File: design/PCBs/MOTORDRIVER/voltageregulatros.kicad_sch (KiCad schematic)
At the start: 0 parts

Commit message: worked on motor pcb
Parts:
- added U2: ADP1108AN-3.3, Package_DIP:DIP-8_W7.62mm, symbol Regulator_Switching:ADP1108AN-3.3
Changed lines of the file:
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@@
 	(generator_version "8.0")
 	(paper "A4")
+	(global_label "3.3V"
+		(shape input)
+		(at 143.51 77.47 0)
+		(fields_autoplaced yes)
+		(effects
+			(font
+				(size 1.27 1.27)
+			)
+			(justify left)
+		)
+		(property "Intersheetrefs" "${INTERSHEET_REFS}"
+			(at 150.5409 77.47 0)
+			(effects
+				(font
+					(size 1.27 1.27)
+				)
+				(justify left)
+				(hide yes)
+			)
+		)
+	)
+	(global_label "12V"
+		(shape input)
+		(at 125.73 81.28 180)
+		(fields_autoplaced yes)
+		(effects
+			(font
+				(size 1.27 1.27)
+			)
+			(justify right)
+		)
+		(property "Intersheetrefs" "${INTERSHEET_REFS}"
+			(at 119.7661 81.28 0)
+			(effects
+				(font
+					(size 1.27 1.27)
+				)
+				(justify right)
+				(hide yes)
+			)
+		)
+	)
+	(symbol
+		(lib_id "Regulator_Switching:ADP1108AN-3.3")
+		(at 142.24 96.52 0)
+		(unit 1)
+		(exclude_from_sim no)
+		(in_bom yes)
+		(on_board yes)
+		(dnp no)
+		(fields_autoplaced yes)
+		(property "Reference" "U2"
+			(at 125.73 89.5855 0)
+			(effects
+				(font
+					(size 1.27 1.27)
+				)
+			)
+		)
+		(property "Value" "ADP1108AN-3.3"
+			(at 125.73 92.1255 0)
+			(effects
+				(font
+					(size 1.27 1.27)
+				)
+			)
+		)
+		(property "Footprint" "Package_DIP:DIP-8_W7.62mm"
+			(at 143.51 105.41 0)
+			(effects
+				(font
+					(size 1.27 1.27)
+				)
+				(justify left)
+				(hide yes)
+			)
+		)
+		(property "Datasheet" "https://www.analog.com/media/en/technical-documentation/data-sheets/ADP1108.pdf"
+			(at 137.16 81.28 0)
+			(effects
+				(font
+					(size 1.27 1.27)
+				)
+				(hide yes)
+			)
+		)
+		(property "Description" "Micropower DC-DC converter, step-up or step-down operation, 2V-30Vin, 3.3V fixed output voltage, DIP-8"
+			(at 142.24 96.52 0)
+			(effects
+				(font
+					(size 1.27 1.27)
+				)
+				(hide yes)
+			)
+		)
+		(pin "7"
+		)
+		(pin "1"
+		)
+		(pin "2"
+		)
+		(pin "5"
+		)
+		(pin "4"
+		)
+		(pin "3"
+		)
+		(pin "6"
+		)
+		(pin "8"
+		)
+		(instances
+			(project ""
+				(path "/c7634e88-16d1-45ec-9aac-9c841e03cf6d/40fe2217-7020-4fd5-b361-1423767f0697"
+					(reference "U2")
+					(unit 1)
+				)
+			)
+		)
+	)
 )

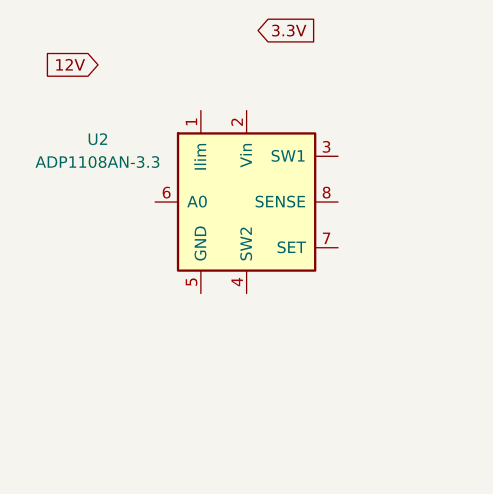
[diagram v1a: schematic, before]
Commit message: moved controller pcb to a single unified pcb, added more work on motordriver
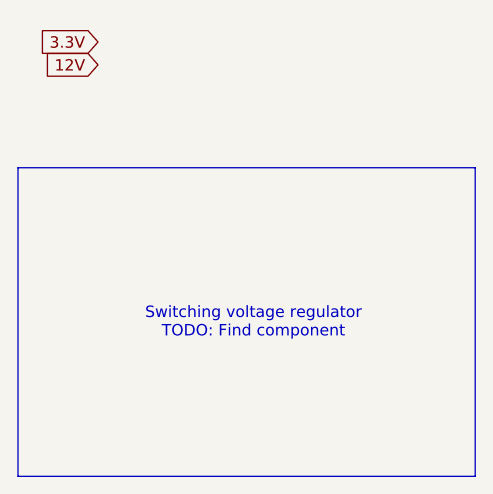
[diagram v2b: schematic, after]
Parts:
- removed U2: ADP1108AN-3.3, Package_DIP:DIP-8_W7.62mm, symbol Regulator_Switching:ADP1108AN-3.3
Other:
- note added: "Switching voltage regulator TODO: Find component"
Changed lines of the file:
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@@
 	(generator_version "8.0")
 	(paper "A4")
+	(rectangle
+		(start 116.84 92.71)
+		(end 167.64 127)
+		(stroke
+			(width 0)
+			(type default)
+		)
+		(fill
+			(type none)
+		)
+	)
+	(text "Switching voltage regulator\nTODO: Find component"
+		(exclude_from_sim no)
+		(at 143.002 109.982 0)
+		(effects
+			(font
+				(size 1.27 1.27)
+			)
+		)
+	)
 	(global_label "3.3V"
 		(shape input)
-		(at 143.51 77.47 0)
+		(at 125.73 78.74 180)
 		(fields_autoplaced yes)
 		(effects
@@
 				(size 1.27 1.27)
 			)
-			(justify left)
+			(justify right)
 		)
 		(property "Intersheetrefs" "${INTERSHEET_REFS}"
-			(at 150.5409 77.47 0)
+			(at 118.6991 78.74 0)
 			(effects
 				(font
 					(size 1.27 1.27)
 				)
-				(justify left)
+				(justify right)
 				(hide yes)
 			)
@@
 			)
 		)
-	)
-	(symbol
-		(lib_id "Regulator_Switching:ADP1108AN-3.3")
-		(at 142.24 96.52 0)
-		(unit 1)
-		(exclude_from_sim no)
-		(in_bom yes)
-		(on_board yes)
-		(dnp no)
-		(fields_autoplaced yes)
-		(property "Reference" "U2"
-			(at 125.73 89.5855 0)
-			(effects
-				(font
-					(size 1.27 1.27)
-				)
-			)
-		)
-		(property "Value" "ADP1108AN-3.3"
-			(at 125.73 92.1255 0)
-			(effects
-				(font
-					(size 1.27 1.27)
-				)
-			)
-		)
-		(property "Footprint" "Package_DIP:DIP-8_W7.62mm"
-			(at 143.51 105.41 0)
-			(effects
-				(font
-					(size 1.27 1.27)
-				)
-				(justify left)
-				(hide yes)
-			)
-		)
-		(property "Datasheet" "https://www.analog.com/media/en/technical-documentation/data-sheets/ADP1108.pdf"
-			(at 137.16 81.28 0)
-			(effects
-				(font
-					(size 1.27 1.27)
-				)
-				(hide yes)
-			)
-		)
-		(property "Description" "Micropower DC-DC converter, step-up or step-down operation, 2V-30Vin, 3.3V fixed output voltage, DIP-8"
-			(at 142.24 96.52 0)
-			(effects
-				(font
-					(size 1.27 1.27)
-				)
-				(hide yes)
-			)
-		)
-		(pin "7"
-		)
-		(pin "1"
-		)
-		(pin "2"
-		)
-		(pin "5"
-		)
-		(pin "4"
-		)
-		(pin "3"
-		)
-		(pin "6"
-		)
-		(pin "8"
-		)
-		(instances
-			(project ""
-				(path "/c7634e88-16d1-45ec-9aac-9c841e03cf6d/40fe2217-7020-4fd5-b361-1423767f0697"
-					(reference "U2")
-					(unit 1)
-				)
-			)
-		)

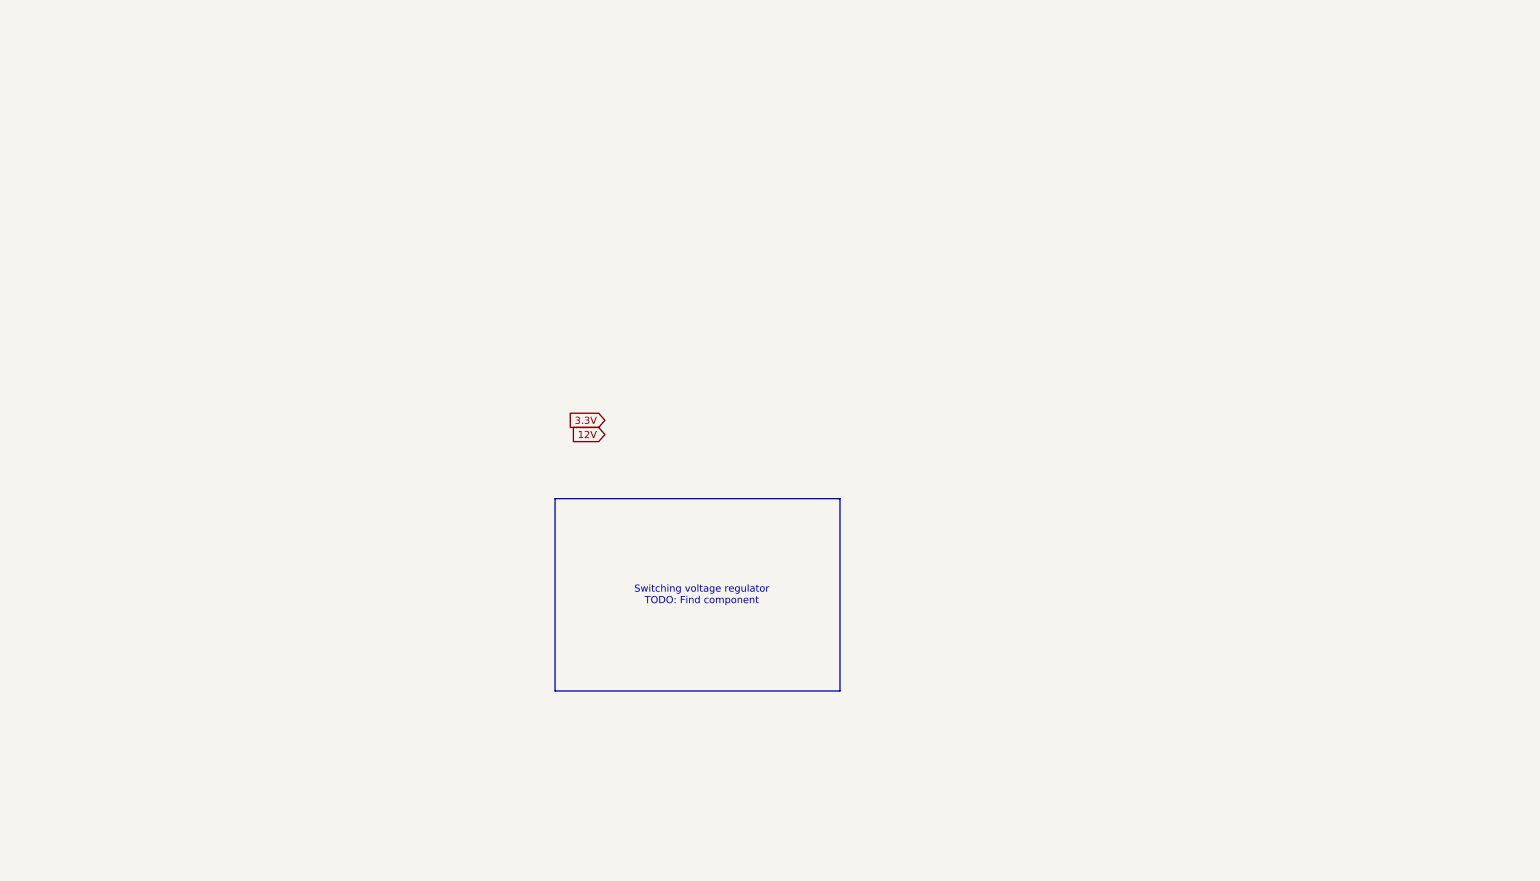
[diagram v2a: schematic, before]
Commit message: 12 to 3.3 LDO added, temporary 5 to 12 reg added
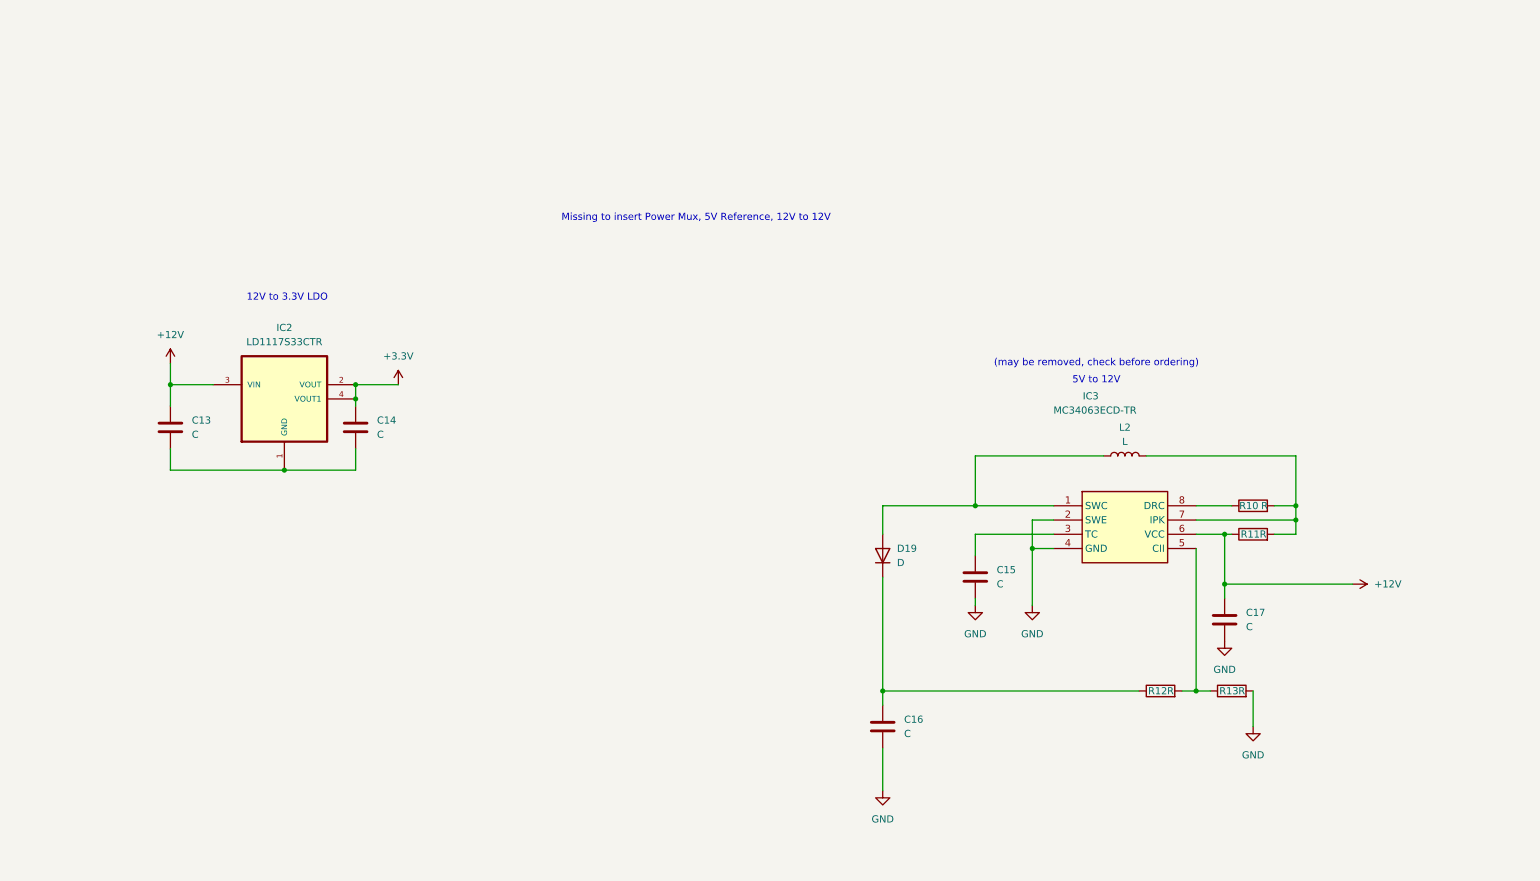
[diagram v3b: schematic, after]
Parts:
- added C13, C14, C15, C16, C17: C, symbol Device:C
- added D19: D, symbol Device:D
- added IC2: LD1117S33CTR, LD1117S33CTR:SOT223, symbol LD1117S33CTR:LD1117S33CTR
- added IC3: MC34063ECD-TR, SOIC127P600X175-8N, symbol MC34063ECD-TR:MC34063ECD-TR
- added L2: L, symbol Device:L
- added R10, R11, R12, R13: R, symbol Device:R
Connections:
- new net: C13.2, C14.2, IC2.1 (GND)
- new net: C16.1, D19.1 (K), R12.1
- new net: D19.2 (A), IC3.1 (SWC), L2.1
- new net: C15.1, IC3.3 (TC)
- new net: IC3.5 (CII), R12.2, R13.1
- new net: IC3.7 (IPK), L2.2, R10.2, R11.2
- new net: IC3.8 (DRC), R10.1
- new net +12V: C13.1, C17.1, IC2.3 (VIN), IC3.6 (VCC), R11.1
- new net +3.3V: C14.1, IC2.2 (VOUT), IC2.4 (VOUT1)
- new net GND: C15.2, C16.2, C17.2, IC3.2 (SWE), IC3.4 (GND), R13.2
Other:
- note added: "(may be removed, check before ordering)"
- note added: "12V to 3.3V LDO"
- note added: "5V to 12V"
- note added: "Missing to insert Power Mux, 5V Reference, 12V to 12V"
- note removed: "Switching voltage regulator TODO: Find component"

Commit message: added battery charger
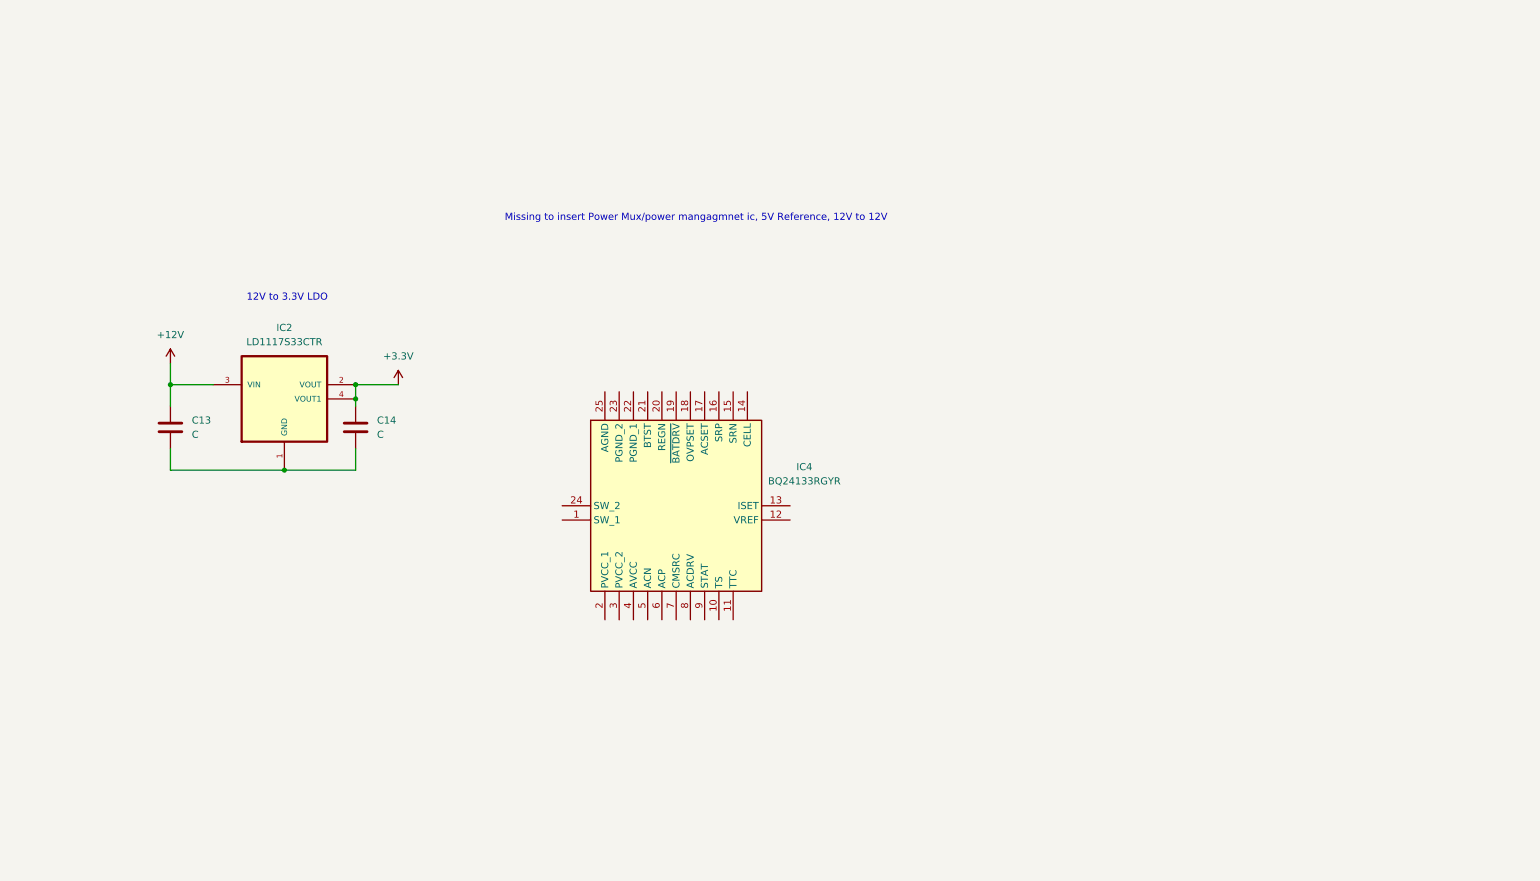
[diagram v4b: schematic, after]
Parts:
- removed C15, C16, C17: C, symbol Device:C
- removed D19: D, symbol Device:D
- removed IC3: MC34063ECD-TR, SOIC127P600X175-8N, symbol MC34063ECD-TR:MC34063ECD-TR
- removed L2: L, symbol Device:L
- removed R10, R11, R12, R13: R, symbol Device:R
- added IC4: BQ24133RGYR, BQ24133RGYR, symbol BQ24133RGYR:BQ24133RGYR
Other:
- note added: "Missing to insert Power Mux/power mangagmnet ic, 5V Reference, 12V to 12V"
- note removed: "(may be removed, check before ordering)"
- note removed: "5V to 12V"
- note removed: "Missing to insert Power Mux, 5V Reference, 12V to 12V"

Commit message: 5V ref IC changed to correct one
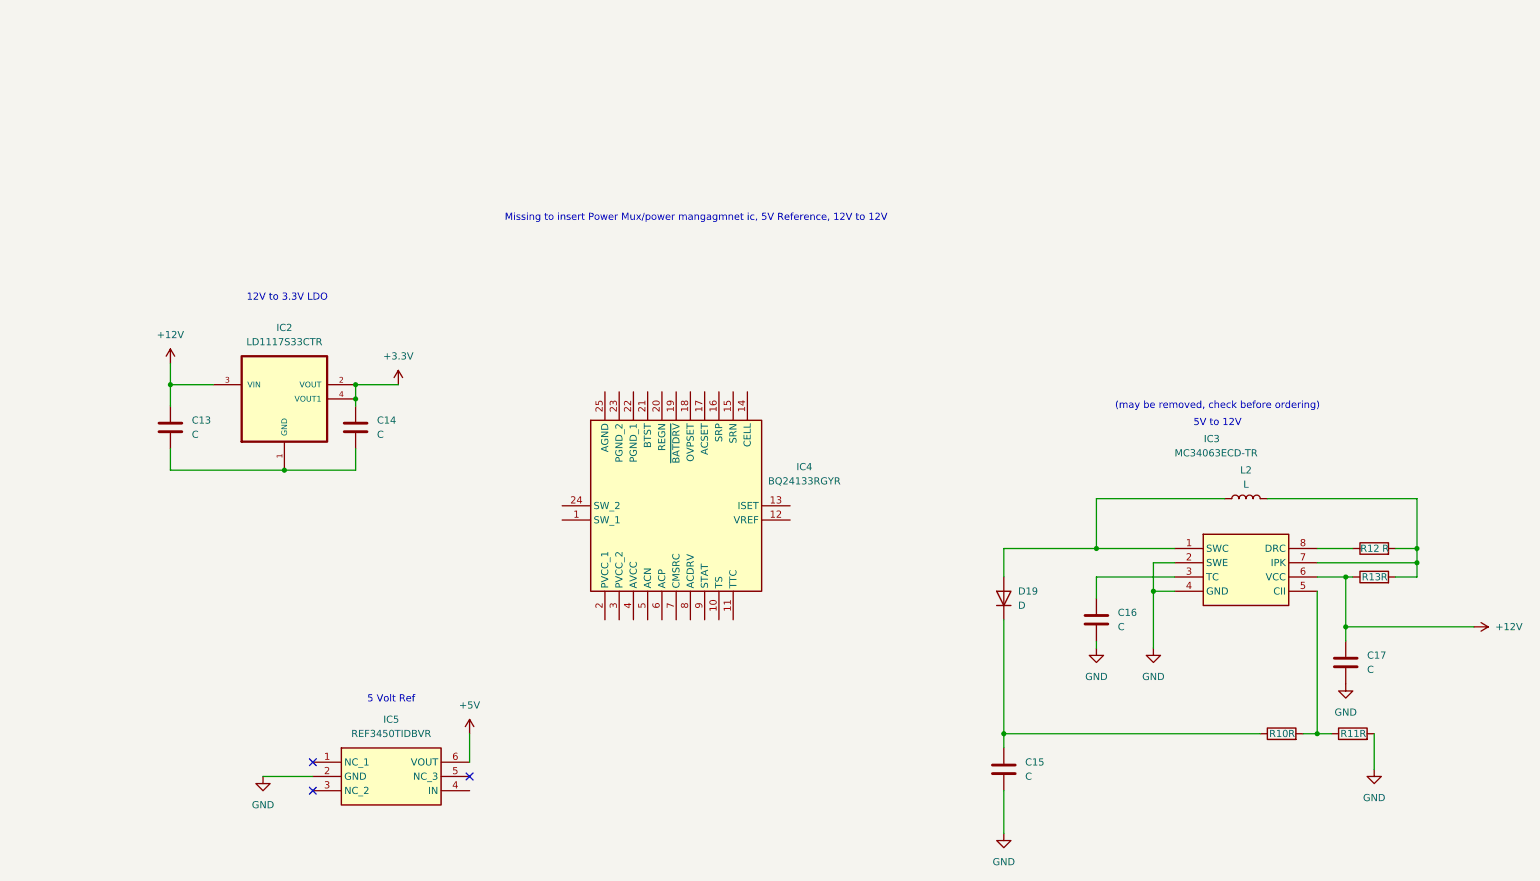
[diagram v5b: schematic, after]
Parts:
- added C15, C16, C17: C, symbol Device:C
- added D19: D, symbol Device:D
- added IC3: MC34063ECD-TR, SOIC127P600X175-8N, symbol MC34063ECD-TR:MC34063ECD-TR
- added IC5: REF3450TIDBVR, SOT95P280X145-6N, symbol REF3450TIDBVR:REF3450TIDBVR
- added L2: L, symbol Device:L
- added R10, R11, R12, R13: R, symbol Device:R
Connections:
- net +12V: now also C17.1, IC3.6 (VCC), R13.1
- new net: D19.2 (A), IC3.1 (SWC), L2.1
- new net: IC3.7 (IPK), L2.2, R12.2, R13.2
- new net: C16.1, IC3.3 (TC)
- new net: IC3.5 (CII), R10.2, R11.1
- new net: IC3.8 (DRC), R12.1
- new net: C15.1, D19.1 (K), R10.1
- new net +5V: IC5.6 (VOUT)
- new net GND: C15.2, C16.2, C17.2, IC3.2 (SWE), IC3.4 (GND), IC5.2 (GND), R11.2
- no-connect marks 0 -> 3
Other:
- note added: "(may be removed, check before ordering)"
- note added: "5 Volt Ref"
- note added: "5V to 12V"
